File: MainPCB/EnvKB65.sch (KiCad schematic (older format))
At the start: 159 parts, among them U1 Pico

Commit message: General cleanup and testing of improved Gerber generation
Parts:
- D_0, D_1, D_10, D_11, D_12, D_13, D_14, D_15, D_16, D_17, D_18, D_19, D_2, D_20, D_21, D_22, D_23, D_24, D_25, D_26, D_27, D_28, D_29, D_3, D_30, D_31, D_32, D_33, D_34, D_35, D_36, D_37, D_38, D_39, D_4, D_40, D_41, D_42, D_43, D_44, D_45, D_46, D_47, D_48, D_49, D_5, D_50, D_51, D_52, D_53, D_54, D_55, D_56, D_57, D_58, D_59, D_6, D_60, D_61, D_62, D_63, D_64, D_65, D_66, D_67, D_68, D_69, D_7, D_70, D_71, D_72, D_73, D_74, D_75, D_8, D_9: LCSC part (none) -> C727111

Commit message: Added ANSI support, generated Gerbers and sent to JLCPCB
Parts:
- removed D_14, D_15, D_30, D_31, D_45, D_46: Diode SOD-323, Diode_SMD:D_SOD-323_HandSoldering, symbol Device:D_Small
- removed K_14, K_15, K_30, K_31, K_45, K_46: KEYSW, MX_Only:MXOnly-1U-NoLED, symbol MX_Alps_Hybrid:MX-NoLED
- added D_27: Diode SOD-323, Diode_SMD:D_SOD-323_HandSoldering, symbol Device:D_Small
- added K_27: KEYSW, MX_Only:MXOnly-1.5U-NoLED, symbol MX_Alps_Hybrid:MX-NoLED
- added K_28, K_43: KEYSW, MX_Only:MXOnly-2.25U-NoLED, symbol MX_Alps_Hybrid:MX-NoLED
- renumbered D_16 to D_14, D_17 to D_15, D_18 to D_16, D_19 to D_17, D_20 to D_18, D_21 to D_19, D_22 to D_20, D_23 to D_21, D_24 to D_22, D_25 to D_23, D_26 to D_24, D_27 to D_25, D_28 to D_26, D_32 to D_28, D_33 to D_29, D_34 to D_30, D_35 to D_31, D_36 to D_32, D_37 to D_33, D_38 to D_34, D_39 to D_35, D_40 to D_36, D_41 to D_37, D_42 to D_38, D_43 to D_39, D_44 to D_40, D_29 to D_41, D_47 to D_42, D_48 to D_43, D_49 to D_44, D_50 to D_45, D_51 to D_46, D_52 to D_47, D_53 to D_48, D_54 to D_49, D_55 to D_50, D_56 to D_51, D_57 to D_52, D_58 to D_53, D_59 to D_54, D_60 to D_55, D_61 to D_56, D_62 to D_57, D_63 to D_58, D_64 to D_59, D_65 to D_60, D_66 to D_61, D_67 to D_62, D_68 to D_63, D_69 to D_64, D_70 to D_65, D_71 to D_66, D_72 to D_67, D_73 to D_68, D_74 to D_69, D_75 to D_70, H1 to H0, H2 to H1, H3 to H2, H4 to H3, H5 to H4, H6 to H5, K_16 to K_14, K_17 to K_15, K_18 to K_16, K_19 to K_17, K_20 to K_18, K_21 to K_19, K_22 to K_20, K_23 to K_21, K_24 to K_22, K_25 to K_23, K_26 to K_24, K_27 to K_25, K_28 to K_26, K_32 to K_29, K_33 to K_30, K_34 to K_31, K_35 to K_32, K_36 to K_33, K_37 to K_34, K_38 to K_35, K_39 to K_36, K_40 to K_37, K_41 to K_38, K_42 to K_39, K_43 to K_40, K_44 to K_41, K_29 to K_42, K_47 to K_44, K_48 to K_45, K_49 to K_46, K_50 to K_47, K_51 to K_48, K_52 to K_49, K_53 to K_50, K_54 to K_51, K_55 to K_52, K_56 to K_53, K_57 to K_54, K_58 to K_55, K_59 to K_56, K_60 to K_57, K_61 to K_58, K_62 to K_59, K_63 to K_60, K_64 to K_61, K_65 to K_62, K_66 to K_63, K_67 to K_64, K_68 to K_65, K_69 to K_66, K_70 to K_67, K_71 to K_68, K_72 to K_69, K_73 to K_70, K_74 to K_71, K_75 to K_72, U1 to U0
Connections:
- net col0: now also K_43.1 (COL)
- net col14: now also K_27.1 (COL), K_28.1 (COL)
- net row1: now also D_27.1 (K)
- net at D_41.2 (A), K_42.2 (ROW): now also K_28.2 (ROW)
- net at D_42.2 (A), K_44.2 (ROW): now also K_43.2 (ROW)
- new net: D_27.2 (A), K_27.2 (ROW)
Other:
- note added: "The duplicated Switch here is intentional\nits for ANSI Enter"
- note added: "This is ANSI Backslash"
- note added: "This is for the ANSI Wide L-shift"

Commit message: replaced all mount holes with versions that have pads
I did this because the pcb can get scraped up if you take it apart a bunch of times to clean it, hopefully this mitigates that.
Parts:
- H0, H1, H2, H3, H4, H5: footprint MountingHole:MountingHole_2.2mm_M2 -> MountingHole:MountingHole_2.2mm_M2_Pad
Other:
- moved on the sheet: H0, H1, H2, H3, H4, H5
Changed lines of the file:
@@
 EELAYER 30 0
 EELAYER END
-$Descr A2 23386 16535
+$Descr User 23622 7874
 encoding utf-8
 Sheet 1 1
@@
 L Mechanical:MountingHole H0
 U 1 1 60AC66FB
-P 4850 6150
-F 0 "H0" H 4950 6196 50  0000 L CNN
-F 1 "MountingHole" H 4950 6105 50  0000 L CNN
-F 2 "MountingHole:MountingHole_2.2mm_M2" H 4850 6150 50  0001 C CNN
-F 3 "~" H 4850 6150 50  0001 C CNN
-F 4 "" H 4850 6150 50  0001 C CNN "LCSC part"
-	1    4850 6150
+P 21350 2800
+F 0 "H0" H 21450 2846 50  0000 L CNN
+F 1 "MountingHole" H 21450 2755 50  0000 L CNN
+F 2 "MountingHole:MountingHole_2.2mm_M2_Pad" H 21350 2800 50  0001 C CNN
+F 3 "~" H 21350 2800 50  0001 C CNN
+F 4 "" H 21350 2800 50  0001 C CNN "LCSC part"
+	1    21350 2800
 	1    0    0    -1
 $EndComp
@@
 L Mechanical:MountingHole H1
 U 1 1 60ACBE92
-P 4850 6350
-F 0 "H1" H 4950 6396 50  0000 L CNN
-F 1 "MountingHole" H 4950 6305 50  0000 L CNN
-F 2 "MountingHole:MountingHole_2.2mm_M2" H 4850 6350 50  0001 C CNN
-F 3 "~" H 4850 6350 50  0001 C CNN
-	1    4850 6350
+P 21350 3000
+F 0 "H1" H 21450 3046 50  0000 L CNN
+F 1 "MountingHole" H 21450 2955 50  0000 L CNN
+F 2 "MountingHole:MountingHole_2.2mm_M2_Pad" H 21350 3000 50  0001 C CNN
+F 3 "~" H 21350 3000 50  0001 C CNN
+	1    21350 3000
 	1    0    0    -1
 $EndComp
@@
 L Mechanical:MountingHole H2
 U 1 1 60AE412B
-P 4850 6550
-F 0 "H2" H 4950 6596 50  0000 L CNN
-F 1 "MountingHole" H 4950 6505 50  0000 L CNN
-F 2 "MountingHole:MountingHole_2.2mm_M2" H 4850 6550 50  0001 C CNN
-F 3 "~" H 4850 6550 50  0001 C CNN
-	1    4850 6550
+P 21350 3200
+F 0 "H2" H 21450 3246 50  0000 L CNN
+F 1 "MountingHole" H 21450 3155 50  0000 L CNN
+F 2 "MountingHole:MountingHole_2.2mm_M2_Pad" H 21350 3200 50  0001 C CNN
+F 3 "~" H 21350 3200 50  0001 C CNN
+	1    21350 3200
 	1    0    0    -1
 $EndComp
@@
 L Mechanical:MountingHole H3
 U 1 1 60AFC1C3
-P 4850 6750
-F 0 "H3" H 4950 6796 50  0000 L CNN
-F 1 "MountingHole" H 4950 6705 50  0000 L CNN
-F 2 "MountingHole:MountingHole_2.2mm_M2" H 4850 6750 50  0001 C CNN
-F 3 "~" H 4850 6750 50  0001 C CNN
-	1    4850 6750
+P 21350 3400
+F 0 "H3" H 21450 3446 50  0000 L CNN
+F 1 "MountingHole" H 21450 3355 50  0000 L CNN
+F 2 "MountingHole:MountingHole_2.2mm_M2_Pad" H 21350 3400 50  0001 C CNN
+F 3 "~" H 21350 3400 50  0001 C CNN
+	1    21350 3400
 	1    0    0    -1
 $EndComp
@@
 L Mechanical:MountingHole H4
 U 1 1 60B142B5
-P 4850 6950
-F 0 "H4" H 4950 6996 50  0000 L CNN
-F 1 "MountingHole" H 4950 6905 50  0000 L CNN
-F 2 "MountingHole:MountingHole_2.2mm_M2" H 4850 6950 50  0001 C CNN
-F 3 "~" H 4850 6950 50  0001 C CNN
-	1    4850 6950
+P 21350 3600
+F 0 "H4" H 21450 3646 50  0000 L CNN
+F 1 "MountingHole" H 21450 3555 50  0000 L CNN
+F 2 "MountingHole:MountingHole_2.2mm_M2_Pad" H 21350 3600 50  0001 C CNN
+F 3 "~" H 21350 3600 50  0001 C CNN
+	1    21350 3600
 	1    0    0    -1
 $EndComp
@@
 L Mechanical:MountingHole H5
 U 1 1 60B2C4B8
-P 4850 7150
-F 0 "H5" H 4950 7196 50  0000 L CNN
-F 1 "MountingHole" H 4950 7105 50  0000 L CNN
-F 2 "MountingHole:MountingHole_2.2mm_M2" H 4850 7150 50  0001 C CNN
-F 3 "~" H 4850 7150 50  0001 C CNN
-	1    4850 7150
-	1    0    0    -1
-$EndComp
+P 21350 3800
+F 0 "H5" H 21450 3846 50  0000 L CNN
+F 1 "MountingHole" H 21450 3755 50  0000 L CNN
+F 2 "MountingHole:MountingHole_2.2mm_M2_Pad" H 21350 3800 50  0001 C CNN
+F 3 "~" H 21350 3800 50  0001 C CNN
+	1    21350 3800
+	1    0    0    -1
+$EndComp

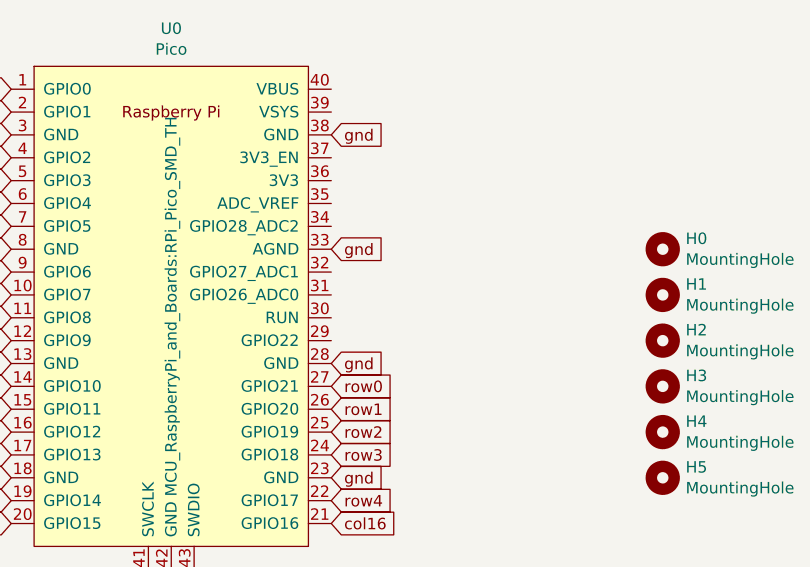
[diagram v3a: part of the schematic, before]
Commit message: See List
* removed RP2040 and atmega32u4 versions
* updated main PCB to have larger holes
* fixed some stuff on the main PCB and added some labels
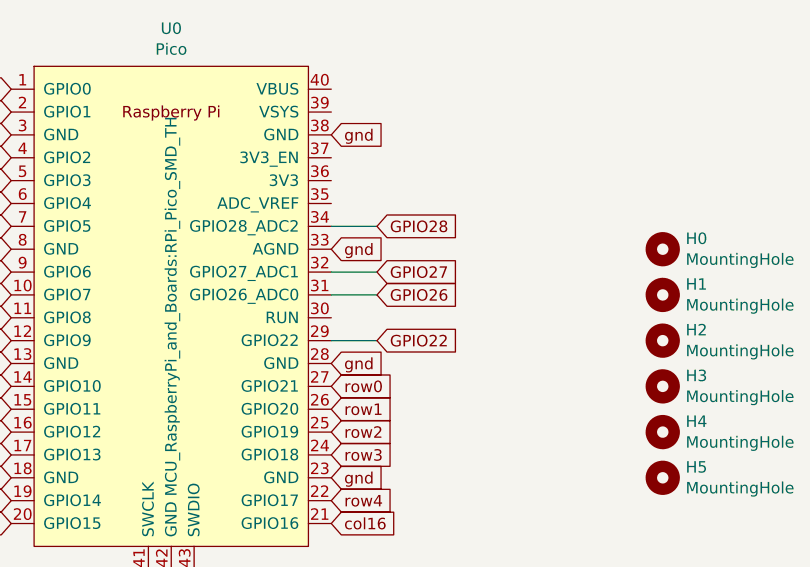
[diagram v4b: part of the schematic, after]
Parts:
- H0, H1, H2, H3, H4, H5: footprint MountingHole:MountingHole_2.2mm_M2_Pad -> MountingHole:MountingHole_4.3mm_M4
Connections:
- net GPIO22: now reaches U0.29 (GPIO22)
- net GPIO26: now reaches U0.31 (GPIO26_ADC0)
- net GPIO27: now reaches U0.32 (GPIO27_ADC1)
- net GPIO28: now reaches U0.34 (GPIO28_ADC2)
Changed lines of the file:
@@
 F 0 "H0" H 21450 2846 50  0000 L CNN
 F 1 "MountingHole" H 21450 2755 50  0000 L CNN
-F 2 "MountingHole:MountingHole_2.2mm_M2_Pad" H 21350 2800 50  0001 C CNN
+F 2 "MountingHole:MountingHole_4.3mm_M4" H 21350 2800 50  0001 C CNN
 F 3 "~" H 21350 2800 50  0001 C CNN
 F 4 "" H 21350 2800 50  0001 C CNN "LCSC part"
@@
 F 0 "H1" H 21450 3046 50  0000 L CNN
 F 1 "MountingHole" H 21450 2955 50  0000 L CNN
-F 2 "MountingHole:MountingHole_2.2mm_M2_Pad" H 21350 3000 50  0001 C CNN
+F 2 "MountingHole:MountingHole_4.3mm_M4" H 21350 3000 50  0001 C CNN
 F 3 "~" H 21350 3000 50  0001 C CNN
 	1    21350 3000
@@
 F 0 "H2" H 21450 3246 50  0000 L CNN
 F 1 "MountingHole" H 21450 3155 50  0000 L CNN
-F 2 "MountingHole:MountingHole_2.2mm_M2_Pad" H 21350 3200 50  0001 C CNN
+F 2 "MountingHole:MountingHole_4.3mm_M4" H 21350 3200 50  0001 C CNN
 F 3 "~" H 21350 3200 50  0001 C CNN
 	1    21350 3200
@@
 F 0 "H3" H 21450 3446 50  0000 L CNN
 F 1 "MountingHole" H 21450 3355 50  0000 L CNN
-F 2 "MountingHole:MountingHole_2.2mm_M2_Pad" H 21350 3400 50  0001 C CNN
+F 2 "MountingHole:MountingHole_4.3mm_M4" H 21350 3400 50  0001 C CNN
 F 3 "~" H 21350 3400 50  0001 C CNN
 	1    21350 3400
@@
 F 0 "H4" H 21450 3646 50  0000 L CNN
 F 1 "MountingHole" H 21450 3555 50  0000 L CNN
-F 2 "MountingHole:MountingHole_2.2mm_M2_Pad" H 21350 3600 50  0001 C CNN
+F 2 "MountingHole:MountingHole_4.3mm_M4" H 21350 3600 50  0001 C CNN
 F 3 "~" H 21350 3600 50  0001 C CNN
 	1    21350 3600
@@
 F 0 "H5" H 21450 3846 50  0000 L CNN
 F 1 "MountingHole" H 21450 3755 50  0000 L CNN
-F 2 "MountingHole:MountingHole_2.2mm_M2_Pad" H 21350 3800 50  0001 C CNN
+F 2 "MountingHole:MountingHole_4.3mm_M4" H 21350 3800 50  0001 C CNN
 F 3 "~" H 21350 3800 50  0001 C CNN
 	1    21350 3800
@@
 Wire Wire Line
 	17800 650  17800 3950
+Text GLabel 20100 3200 2    50   Input ~ 0
+GPIO22
+Text GLabel 20100 3000 2    50   Input ~ 0
+GPIO26
+Text GLabel 20100 2900 2    50   Input ~ 0
+GPIO27
+Text GLabel 20100 2700 2    50   Input ~ 0
+GPIO28
+Wire Wire Line
+	19900 3200 20100 3200
+Wire Wire Line
+	19900 3000 20100 3000
+Wire Wire Line
+	20100 2900 19900 2900
+Wire Wire Line
+	19900 2700 20100 2700
 $EndSCHEMATC
